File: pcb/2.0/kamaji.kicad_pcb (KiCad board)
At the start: 2 copper layers, 100 x 100 mm, 92 parts, among them J1 RJ10, J2 RJ10, J3 RJ10, J4 RJ10, J5 RJ10, J6 RJ10, J7 USB_B, J8 USB_A, Q1 2N3904, Q2 IRL540N, Q3 IRL540N, SW1 SW_Push, SW2 SW_Push, SW3 SW_Push, U1 ATMEGA32U4-AU, Y1 16MHz

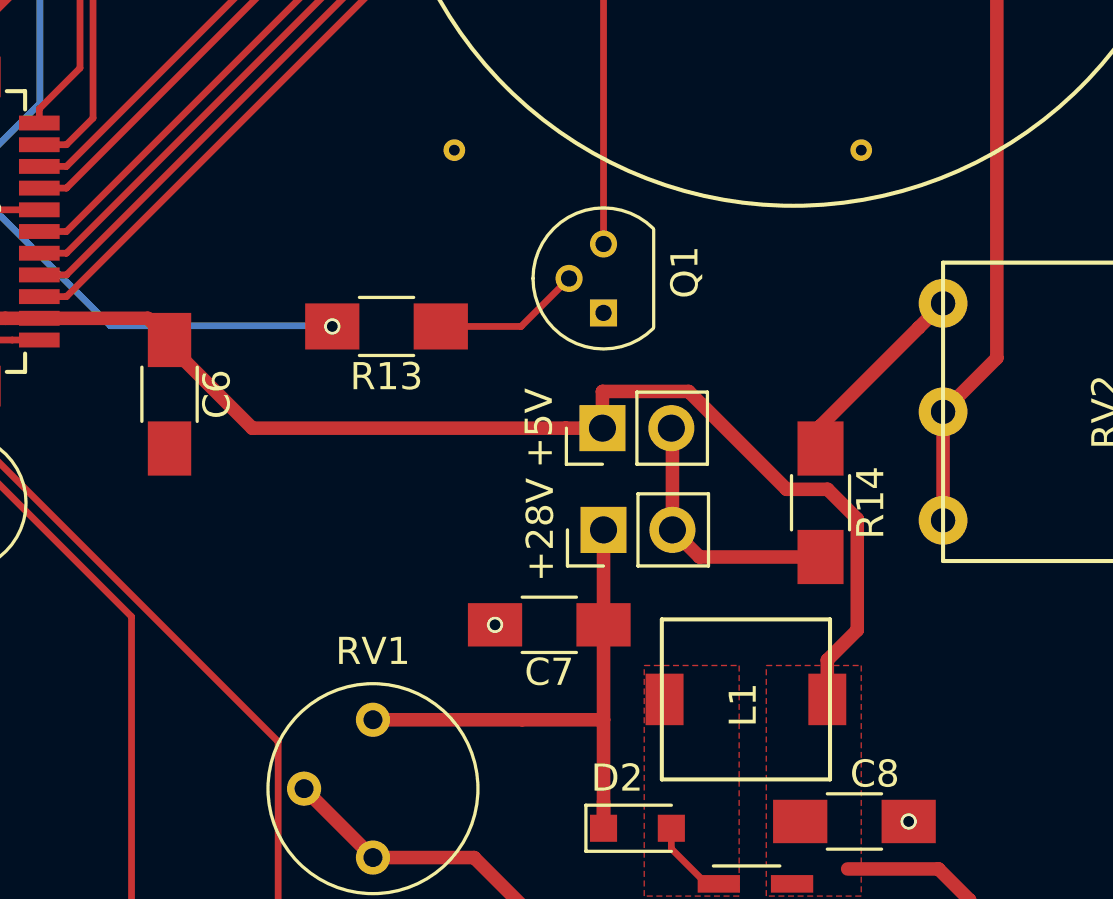
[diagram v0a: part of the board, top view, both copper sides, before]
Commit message: add a jumper for the volume regulator
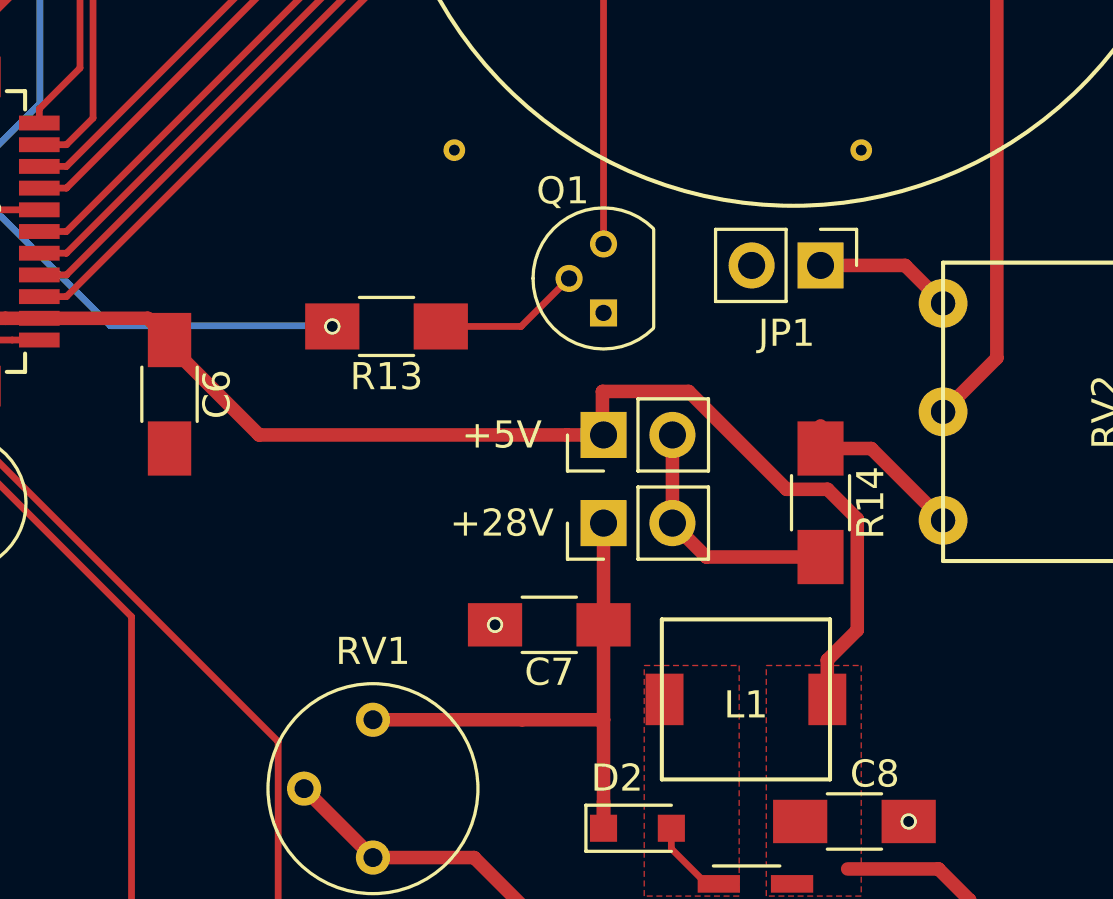
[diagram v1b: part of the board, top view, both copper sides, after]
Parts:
- removed +28V: Jumper_NC_Small, Socket_Strips:Socket_Strip_Straight_1x02_Pitch2.54mm
- removed +5V: SoundVcc2, Socket_Strips:Socket_Strip_Straight_1x02_Pitch2.54mm
- added JP1: Jumper_NO_Small, Pin_Headers:Pin_Header_Straight_1x02_Pitch2.54mm, F.Cu at (133.5, 99.2)
- added JP2: Jumper_NC_Small, Pin_Headers:Pin_Header_Straight_1x02_Pitch2.54mm, F.Cu at (125.5, 108.8)
- added JP3: SoundVcc2, Pin_Headers:Pin_Header_Straight_1x02_Pitch2.54mm, F.Cu at (125.5, 105.5)
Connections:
- RV2 pad 1: Net-(R14-Pad1) -> Net-(JP1-Pad1)
- RV2 pad 3: Net-(LS1-Pad1) -> Net-(R14-Pad1)
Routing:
- net Net-(JP1-Pad1): track 0.00 -> 5.10 mm
- net Net-(LS1-Pad1): track 27.5 -> 23.5 mm
- net Net-(R14-Pad1): track 7.22 -> 6.45 mm
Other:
- board text added: "+28V"
- board text added: "+5V"

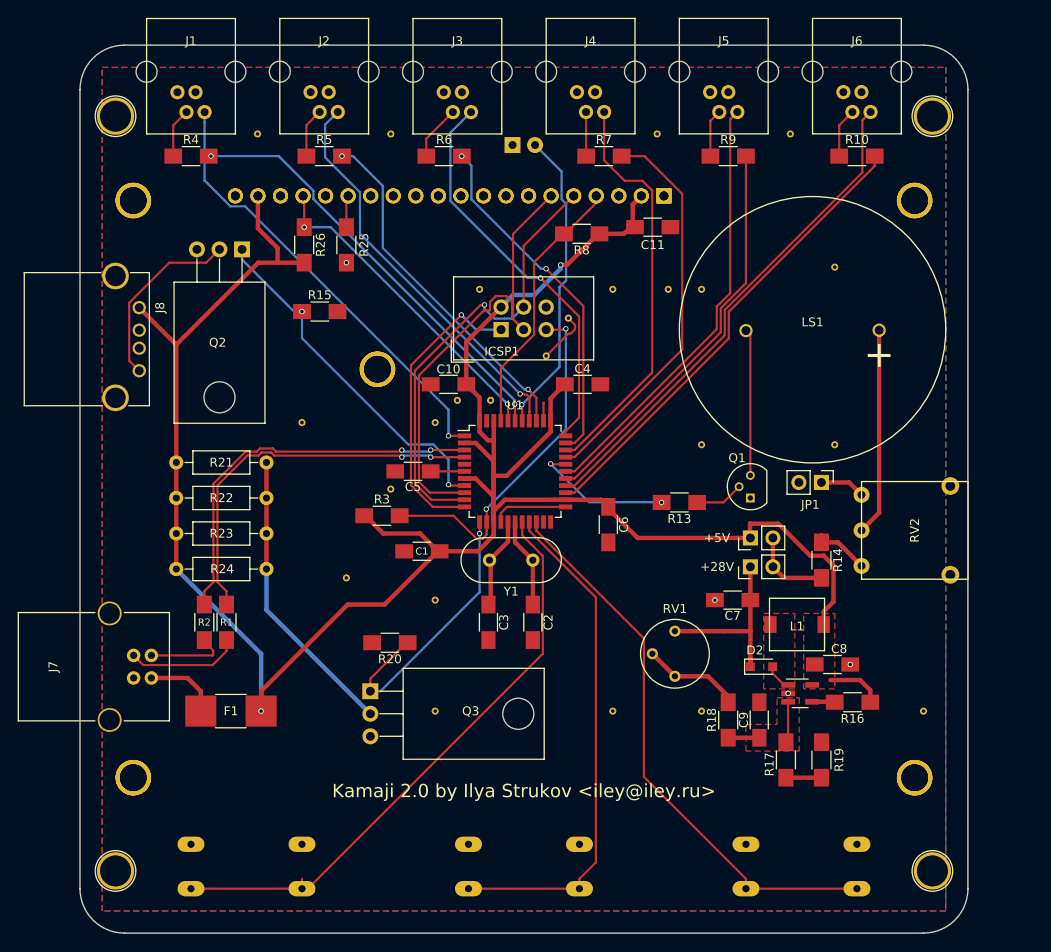
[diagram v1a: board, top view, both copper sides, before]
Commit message: flip the LCD and re-route the board
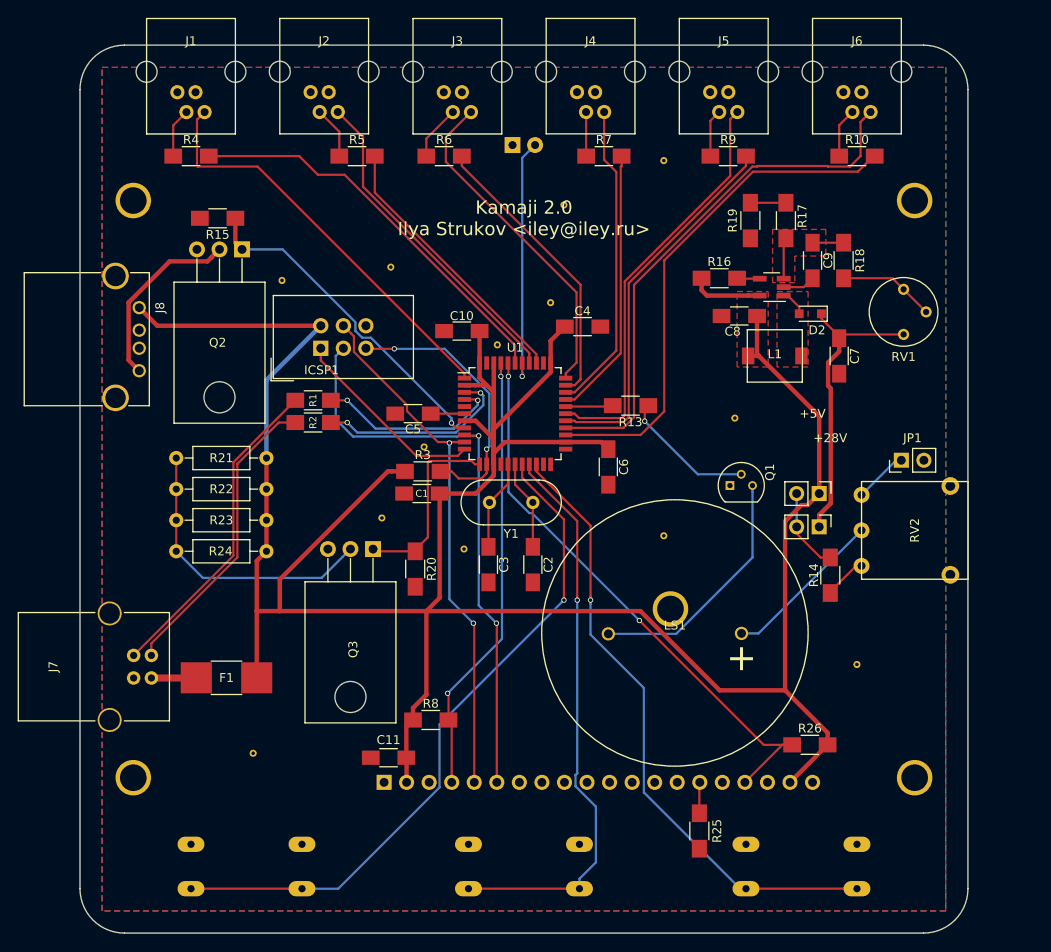
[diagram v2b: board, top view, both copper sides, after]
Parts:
- removed the DS1 at (100.0, 100.0) (x2)
- removed REF** (x4): 1pin, Connectors:1pin
- removed the VIA** at (105.0, 80.8)
- removed the VIA** at (130.0, 60.0)
- removed the VIA** at (135.0, 75.0)
- removed the VIA** at (135.0, 95.0)
- removed the VIA** at (120.0, 95.0)
- removed the VIA** at (116.2, 77.5)
- removed the VIA** at (120.0, 77.5)
- removed the VIA** at (110.0, 77.5)
- removed the VIA** at (96.2, 90.0)
- removed the VIA** at (102.5, 85.0)
- removed the VIA** at (80.0, 110.0)
- removed the VIA** at (145.0, 125.0)
- removed the VIA** at (90.0, 112.5)
- removed the VIA** at (85.0, 100.0)
- removed the VIA** at (92.5, 90.0)
- removed the VIA** at (90.0, 92.5)
- removed the VIA** at (75.0, 92.5)
- removed the VIA** at (120.0, 125.0)
- removed the VIA** at (110.0, 125.0)
- removed the VIA** at (90.0, 125.0)
- removed the VIA** at (70.0, 60.0)
- removed the VIA** at (85.0, 60.0)
- removed the VIA** at (95.0, 77.5)
- removed the VIA** at (115.0, 60.0)
- added DS1: LCD12864B, kamaji:LCD12864, B.Cu at (100.0, 100.0)
- added VIA**: Via_0.8mm, kamaji:Via_0.8mm, F.Cu at (72.8, 76.5)
- added VIA**: Via_0.8mm, kamaji:Via_0.8mm, F.Cu at (88.8, 95.2)
- added VIA**: Via_0.8mm, kamaji:Via_0.8mm, F.Cu at (103.0, 79.0)
- added VIA**: Via_0.8mm, kamaji:Via_0.8mm, F.Cu at (97.0, 83.8)
- added VIA**: Via_0.8mm, kamaji:Via_0.8mm, F.Cu at (85.0, 75.0)
- added VIA**: Via_0.8mm, kamaji:Via_0.8mm, F.Cu at (104.5, 68.0)
- added VIA**: Via_0.8mm, kamaji:Via_0.8mm, F.Cu at (115.8, 63.0)
- added VIA**: Via_0.8mm, kamaji:Via_0.8mm, F.Cu at (115.8, 105.2)
- added VIA**: Via_0.8mm, kamaji:Via_0.8mm, F.Cu at (123.8, 92.0)
- added VIA**: Via_0.8mm, kamaji:Via_0.8mm, F.Cu at (137.5, 119.8)
- added VIA**: Via_0.8mm, kamaji:Via_0.8mm, F.Cu at (69.5, 129.8)
- added VIA**: Via_0.8mm, kamaji:Via_0.8mm, F.Cu at (93.2, 106.8)
- added VIA**: Via_0.8mm, kamaji:Via_0.8mm, F.Cu at (84.0, 103.2)
- moved R26 80.1 mm to (132.2, 128.8), turned to 0 degrees
- moved R25 77.0 mm to (119.8, 138.5)
- moved C11 66.7 mm to (84.8, 130.2), turned to 180 degrees
- moved R19 61.3 mm to (125.5, 69.8), turned to 270 degrees
- moved R17 60.8 mm to (129.5, 69.8), turned to 270 degrees
- moved R8 57.3 mm to (89.5, 126.0), turned to 0 degrees
- moved R18 53.4 mm to (136.0, 74.2), turned to 270 degrees
- moved C9 52.1 mm to (132.5, 74.2), turned to 270 degrees
- moved RV1 50.6 mm to (142.8, 77.5), turned to 180 degrees
- moved R16 50.1 mm to (122.0, 76.2), turned to 0 degrees
- moved BC1 45.9 mm to (127.9, 77.2), turned to 180 degrees
- moved C8 40.6 mm to (124.2, 80.5), turned to 180 degrees
- moved D2 40.1 mm to (132.2, 80.2), turned to 180 degrees
- moved LS1 37.5 mm to (117.0, 116.2)
- moved L1 30.4 mm to (128.2, 85.0), turned to 90 degrees
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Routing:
- net VCC: track 267.3 -> 333.2 mm, vias 2 -> 0
- net /LCD_RST: track 36.6 -> 65.4 mm
- net /USBBD-: track 9.08 -> 34.0 mm
- net /USBBD+: track 12.8 -> 36.3 mm
- net /USB_D-: track 45.0 -> 22.3 mm
- net /USB_D+: track 43.6 -> 21.0 mm
- net /LCD_CS: track 29.9 -> 50.0 mm, vias 0 -> 2
- net GND: track 17.4 -> 3.66 mm, vias 4 -> 0
- net /PLED4: track 44.3 -> 30.6 mm
- net /SCK: track 54.0 -> 66.8 mm, vias 0 -> 2
- net /Boost Converter/BOOST_VOUT: track 20.8 -> 33.4 mm
- net /MISO: track 33.7 -> 22.3 mm, vias 1 -> 0
- net /PBTN4: track 46.1 -> 35.1 mm
- net /MOSI: track 50.6 -> 61.6 mm, vias 1 -> 2
- net Net-(LS1-Pad2): track 17.0 -> 27.9 mm
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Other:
- board text added: "Kamaji 2.0 Ilya Strukov <iley@iley.ru>"
- board text removed: "Kamaji 2.0 by Ilya Strukov <iley@iley.ru>"

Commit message: move the speaker
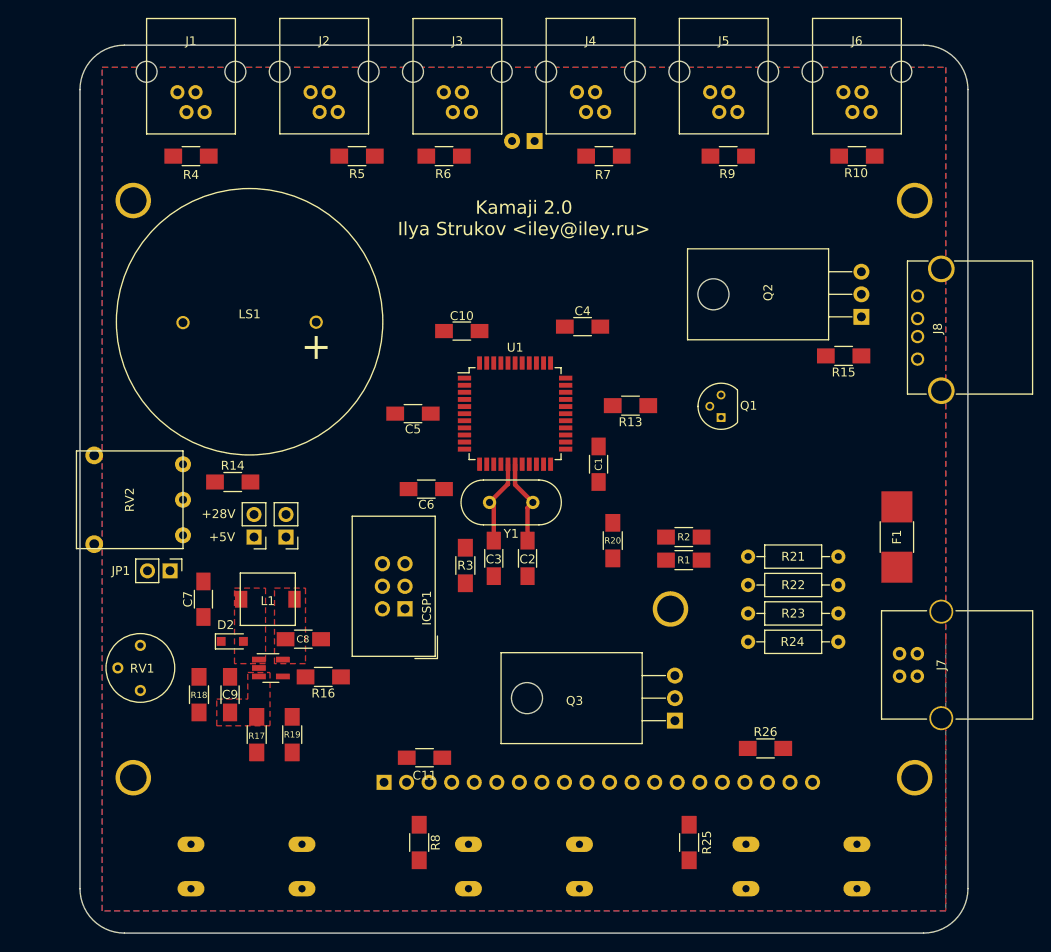
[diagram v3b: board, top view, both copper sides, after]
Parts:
- removed VIA** (x13): Via_0.8mm, kamaji:Via_0.8mm
- moved RV1 97.1 mm to (56.8, 122.7), turned to 0 degrees
- moved RV2 88.5 mm to (55.6, 101.2), turned to 90 degrees
- moved J8 87.9 mm to (144.3, 85.4), turned to 90 degrees
- moved R18 87.5 mm to (63.4, 123.2), turned to 90 degrees
- moved J7 84.3 mm to (142.3, 118.5), turned to 0 degrees
- moved JP1 83.3 mm to (60.1, 109.2), turned to 270 degrees
- moved R17 83.1 mm to (69.9, 127.7), turned to 90 degrees
- moved C9 81.8 mm to (66.9, 123.2), turned to 90 degrees
- moved R19 77.6 mm to (73.9, 127.7), turned to 90 degrees
- moved F1 77.1 mm to (142.0, 105.4), turned to 90 degrees
- moved C7 76.7 mm to (63.9, 112.4), turned to 90 degrees
- moved D2 74.8 mm to (67.2, 117.2), turned to 0 degrees
- moved R15 72.2 mm to (136.0, 85.0)
- moved BC1 70.9 mm to (71.5, 120.2), turned to 0 degrees
- moved Q2 70.2 mm to (138.0, 80.6), turned to 90 degrees
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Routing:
- net VCC: track 333.2 -> 0.00 mm
- net /CBTN1: track 76.9 -> 0.00 mm, vias 1 -> 0
- net /CBTN3: track 70.5 -> 0.00 mm, vias 1 -> 0
- net /SCK: track 66.8 -> 0.00 mm, vias 2 -> 0
- net /LCD_RST: track 65.4 -> 0.00 mm, vias 2 -> 0
- net /CBTN2: track 64.3 -> 0.00 mm, vias 1 -> 0
- net /MOSI: track 61.6 -> 0.00 mm, vias 2 -> 0
- net /PBTN6: track 60.1 -> 0.00 mm
- net /PLED6: track 57.8 -> 0.00 mm
- net /LCD_CS: track 50.0 -> 0.00 mm, vias 2 -> 0
- net /PBTN1: track 46.8 -> 0.00 mm
- net /PBTN5: track 46.4 -> 0.00 mm
- net /PLED1: track 45.3 -> 0.00 mm
- net /PLED5: track 42.2 -> 0.00 mm
- net /PBTN3: track 38.2 -> 0.00 mm
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
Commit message: re-route everything again
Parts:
- moved R3 15.2 mm to (78.3, 110.4)
- moved Q1 8.51 mm to (116.6, 85.5), turned to 180 degrees
- moved R1 5.72 mm to (119.9, 102.6)
- moved R2 5.72 mm to (119.9, 100.0)
- moved R8 1.87 mm to (87.7, 138.0), turned to 0 degrees
- moved C7 1.58 mm to (63.4, 113.9), turned to 180 degrees
- moved LS1 0.95 mm to (70.0, 80.8), turned to 0 degrees
- moved F1 0.32 mm to (142.3, 105.5)
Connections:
- net Net-(Q3-Pad2) renamed /DUMMY-
- U1 pad 18: /CBTN1 -> (no net)
- U1 pad 19: /CBTN2 -> (no net)
- U1 pad 20: /CBTN3 -> /CBTN2
- U1 pad 21: (no net) -> /CBTN3
- U1 pad 22: (no net) -> /LAMP
- U1 pad 8: /LAMP -> /CBTN1
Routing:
- net VCC: track 0.00 -> 264.2 mm
- net /CBTN1: track 0.00 -> 97.2 mm
- net /CBTN3: track 0.00 -> 74.7 mm
- net /CBTN2: track 0.00 -> 62.3 mm
- net /LCD_RST: track 0.00 -> 62.2 mm, vias 0 -> 1
- net /SCK: track 0.00 -> 61.3 mm
- net /MOSI: track 0.00 -> 55.7 mm
- net /LCD_CS: track 0.00 -> 55.4 mm, vias 0 -> 1
- net /PBTN6: track 0.00 -> 55.4 mm
- net /PLED6: track 0.00 -> 51.3 mm
- net /DUMMY_EN: track 0.00 -> 48.2 mm, vias 0 -> 2
- net /PLED1: track 0.00 -> 46.6 mm
- net /PBTN5: track 0.00 -> 46.6 mm
- net /LAMP: track 0.00 -> 46.5 mm, vias 0 -> 1
- net /PBTN1: track 0.00 -> 46.4 mm
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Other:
- net class Default: clearance 0.2 -> 0.1524
- rule trace_clearance: 0.2 -> 0.1524
